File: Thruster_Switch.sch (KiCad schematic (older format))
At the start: 11 parts, among them P1 XT60, P2 XT60, P3 XT60, P4 XT60, Q2 IPD90P03P4L

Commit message: Update Netlist
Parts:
- renumbered D2 to D1, D3 to D2, Q2 to Q1, R3 to R1, R4 to R2, R5 to R3
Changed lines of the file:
@@
 AR Path="/58E6D43E/58E019DD" Ref="P11"  Part="1"
 AR Path="/58E0048C/58E019DD" Ref="P15"  Part="1"
-F 0 "P11" H 6850 4450 50  0000 C CNN
+F 0 "P15" H 6850 4450 50  0000 C CNN
 F 1 "XT60" H 6850 4150 50  0000 C CNN
 F 2 "zeabus:XT60" H 6950 4050 60  0001 C CNN
@@
 $EndComp
 $Comp
-L R R5
+L R R3
 U 1 1 58E01A68
 P 6250 4150
-AR Path="/58E52973/58E01A68" Ref="R5"  Part="1"
-AR Path="/58E62AD5/58E01A68" Ref="R20"  Part="1"
-AR Path="/58E6D43E/58E01A68" Ref="R25"  Part="1"
-AR Path="/58E0048C/58E01A68" Ref="R30"  Part="1"
-F 0 "R25" V 6330 4150 50  0000 C CNN
+AR Path="/58E52973/58E01A68" Ref="R3"  Part="1"
+AR Path="/58E62AD5/58E01A68" Ref="R12"  Part="1"
+AR Path="/58E6D43E/58E01A68" Ref="R15"  Part="1"
+AR Path="/58E0048C/58E01A68" Ref="R18"  Part="1"
+F 0 "R18" V 6330 4150 50  0000 C CNN
 F 1 "10k" V 6250 4150 50  0000 C CNN
 F 2 "Resistors_SMD:R_0603" V 6180 4150 50  0001 C CNN
@@
 $EndComp
 $Comp
-L LED_Small D3
+L LED_Small D2
 U 1 1 58E01A8B
 P 6250 4550
-AR Path="/58E52973/58E01A8B" Ref="D3"  Part="1"
-AR Path="/58E62AD5/58E01A8B" Ref="D10"  Part="1"
-AR Path="/58E6D43E/58E01A8B" Ref="D13"  Part="1"
-AR Path="/58E0048C/58E01A8B" Ref="D16"  Part="1"
-F 0 "D13" H 6200 4675 50  0000 L CNN
+AR Path="/58E52973/58E01A8B" Ref="D2"  Part="1"
+AR Path="/58E62AD5/58E01A8B" Ref="D8"  Part="1"
+AR Path="/58E6D43E/58E01A8B" Ref="D10"  Part="1"
+AR Path="/58E0048C/58E01A8B" Ref="D12"  Part="1"
+F 0 "D12" H 6200 4675 50  0000 L CNN
 F 1 "LED_Small" H 6075 4450 50  0000 L CNN
 F 2 "LEDs:LED_0603" V 6250 4550 50  0001 C CNN
@@
 $EndComp
 $Comp
-L R R3
+L R R1
 U 1 1 58E01FA8
 P 5550 2500
-AR Path="/58E52973/58E01FA8" Ref="R3"  Part="1"
-AR Path="/58E62AD5/58E01FA8" Ref="R18"  Part="1"
-AR Path="/58E6D43E/58E01FA8" Ref="R23"  Part="1"
-AR Path="/58E0048C/58E01FA8" Ref="R28"  Part="1"
-F 0 "R23" V 5630 2500 50  0000 C CNN
+AR Path="/58E52973/58E01FA8" Ref="R1"  Part="1"
+AR Path="/58E62AD5/58E01FA8" Ref="R10"  Part="1"
+AR Path="/58E6D43E/58E01FA8" Ref="R13"  Part="1"
+AR Path="/58E0048C/58E01FA8" Ref="R16"  Part="1"
+F 0 "R16" V 5630 2500 50  0000 C CNN
 F 1 "10k" V 5550 2500 50  0000 C CNN
 F 2 "Resistors_SMD:R_0603" V 5480 2500 50  0001 C CNN
@@
 $EndComp
 $Comp
-L R R4
+L R R2
 U 1 1 58E01FFB
 P 5550 3050
-AR Path="/58E52973/58E01FFB" Ref="R4"  Part="1"
-AR Path="/58E62AD5/58E01FFB" Ref="R19"  Part="1"
-AR Path="/58E6D43E/58E01FFB" Ref="R24"  Part="1"
-AR Path="/58E0048C/58E01FFB" Ref="R29"  Part="1"
-F 0 "R24" V 5630 3050 50  0000 C CNN
+AR Path="/58E52973/58E01FFB" Ref="R2"  Part="1"
+AR Path="/58E62AD5/58E01FFB" Ref="R11"  Part="1"
+AR Path="/58E6D43E/58E01FFB" Ref="R14"  Part="1"
+AR Path="/58E0048C/58E01FFB" Ref="R17"  Part="1"
+F 0 "R17" V 5630 3050 50  0000 C CNN
 F 1 "1k" V 5550 3050 50  0000 C CNN
 F 2 "Resistors_SMD:R_0603" V 5480 3050 50  0001 C CNN
@@
 $EndComp
 $Comp
-L GND #PWR012
+L GND #PWR12
 U 1 1 58E0369B
 P 6250 4800
-AR Path="/58E52973/58E0369B" Ref="#PWR012"  Part="1"
-AR Path="/58E62AD5/58E0369B" Ref="#PWR015"  Part="1"
-AR Path="/58E6D43E/58E0369B" Ref="#PWR016"  Part="1"
-AR Path="/58E0048C/58E0369B" Ref="#PWR017"  Part="1"
-F 0 "#PWR017" H 6250 4550 50  0001 C CNN
+AR Path="/58E52973/58E0369B" Ref="#PWR12"  Part="1"
+AR Path="/58E62AD5/58E0369B" Ref="#PWR15"  Part="1"
+AR Path="/58E6D43E/58E0369B" Ref="#PWR16"  Part="1"
+AR Path="/58E0048C/58E0369B" Ref="#PWR17"  Part="1"
+F 0 "#PWR17" H 6250 4550 50  0001 C CNN
 F 1 "GND" H 6250 4650 50  0000 C CNN
 F 2 "" H 6250 4800 50  0001 C CNN
@@
 AR Path="/58E6D43E/58E0D2A0" Ref="P12"  Part="1"
 AR Path="/58E0048C/58E0D2A0" Ref="P16"  Part="1"
-F 0 "P12" H 7400 4450 50  0000 C CNN
+F 0 "P16" H 7400 4450 50  0000 C CNN
 F 1 "XT60" H 7400 4150 50  0000 C CNN
 F 2 "zeabus:XT60" H 7500 4050 60  0001 C CNN
@@
 AR Path="/58E6D43E/58E0D2E8" Ref="P13"  Part="1"
 AR Path="/58E0048C/58E0D2E8" Ref="P17"  Part="1"
-F 0 "P13" H 7950 4450 50  0000 C CNN
+F 0 "P17" H 7950 4450 50  0000 C CNN
 F 1 "XT60" H 7950 4150 50  0000 C CNN
 F 2 "zeabus:XT60" H 8050 4050 60  0001 C CNN
@@
 AR Path="/58E6D43E/58E0D33F" Ref="P14"  Part="1"
 AR Path="/58E0048C/58E0D33F" Ref="P18"  Part="1"
-F 0 "P14" H 8500 4450 50  0000 C CNN
+F 0 "P18" H 8500 4450 50  0000 C CNN
 F 1 "XT60" H 8500 4150 50  0000 C CNN
 F 2 "zeabus:XT60" H 8600 4050 60  0001 C CNN
@@
 AR Path="/58E6D43E/58E4FE30" Ref="F5"  Part="1"
 AR Path="/58E0048C/58E4FE30" Ref="F6"  Part="1"
-F 0 "F5" V 6330 3550 50  0000 C CNN
+F 0 "F6" V 6330 3550 50  0000 C CNN
 F 1 "Fuse" V 6175 3550 50  0000 C CNN
 F 2 "zeabus:FUSE_AUTO" V 6180 3550 50  0001 C CNN
@@
 	6250 3700 6250 4000
 $Comp
-L Q_PMOS_GDS Q2
+L Q_PMOS_GDS Q1
 U 1 1 58E51C6A
 P 6150 3050
-AR Path="/58E52973/58E51C6A" Ref="Q2"  Part="1"
-AR Path="/58E62AD5/58E51C6A" Ref="Q8"  Part="1"
-AR Path="/58E6D43E/58E51C6A" Ref="Q10"  Part="1"
-AR Path="/58E0048C/58E51C6A" Ref="Q12"  Part="1"
-F 0 "Q10" H 6350 3100 50  0000 L CNN
+AR Path="/58E52973/58E51C6A" Ref="Q1"  Part="1"
+AR Path="/58E62AD5/58E51C6A" Ref="Q4"  Part="1"
+AR Path="/58E6D43E/58E51C6A" Ref="Q5"  Part="1"
+AR Path="/58E0048C/58E51C6A" Ref="Q6"  Part="1"
+F 0 "Q6" H 6350 3100 50  0000 L CNN
 F 1 "IPD90P03P4L" H 6350 3000 50  0000 L CNN
 F 2 "TO_SOT_Packages_SMD:TO-252-2Lead" H 6350 3150 50  0001 C CNN
@@
 $EndComp
 $Comp
-L D_Zener D2
+L D_Zener D1
 U 1 1 58E6427A
 P 5850 2750
-AR Path="/58E52973/58E6427A" Ref="D2"  Part="1"
-AR Path="/58E62AD5/58E6427A" Ref="D9"  Part="1"
-AR Path="/58E6D43E/58E6427A" Ref="D12"  Part="1"
-AR Path="/58E0048C/58E6427A" Ref="D15"  Part="1"
-F 0 "D12" H 5850 2850 50  0000 C CNN
+AR Path="/58E52973/58E6427A" Ref="D1"  Part="1"
+AR Path="/58E62AD5/58E6427A" Ref="D7"  Part="1"
+AR Path="/58E6D43E/58E6427A" Ref="D9"  Part="1"
+AR Path="/58E0048C/58E6427A" Ref="D11"  Part="1"
+F 0 "D11" H 5850 2850 50  0000 C CNN
 F 1 "BZX585-C12" H 5850 2650 50  0000 C CNN
 F 2 "Diodes_SMD:D_SOD-523" H 5850 2750 50  0001 C CNN

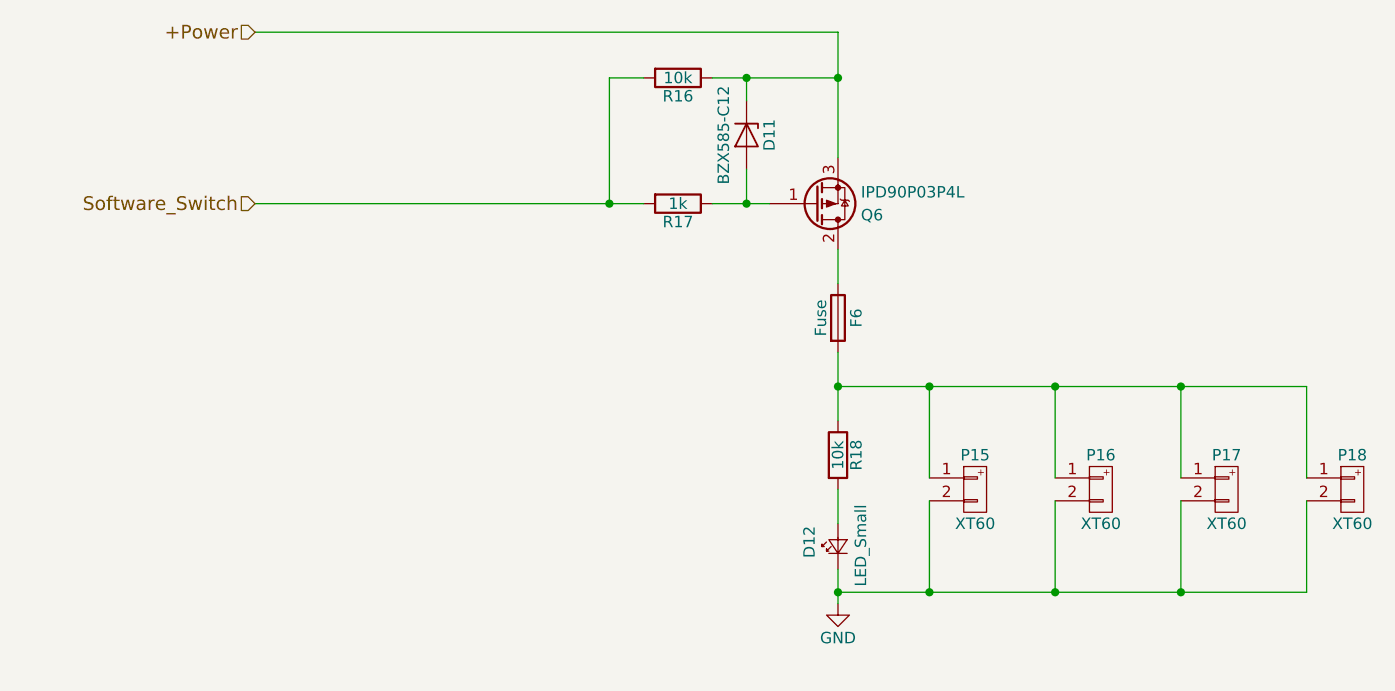
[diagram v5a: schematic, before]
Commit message: Ver1 Power_dist PCB
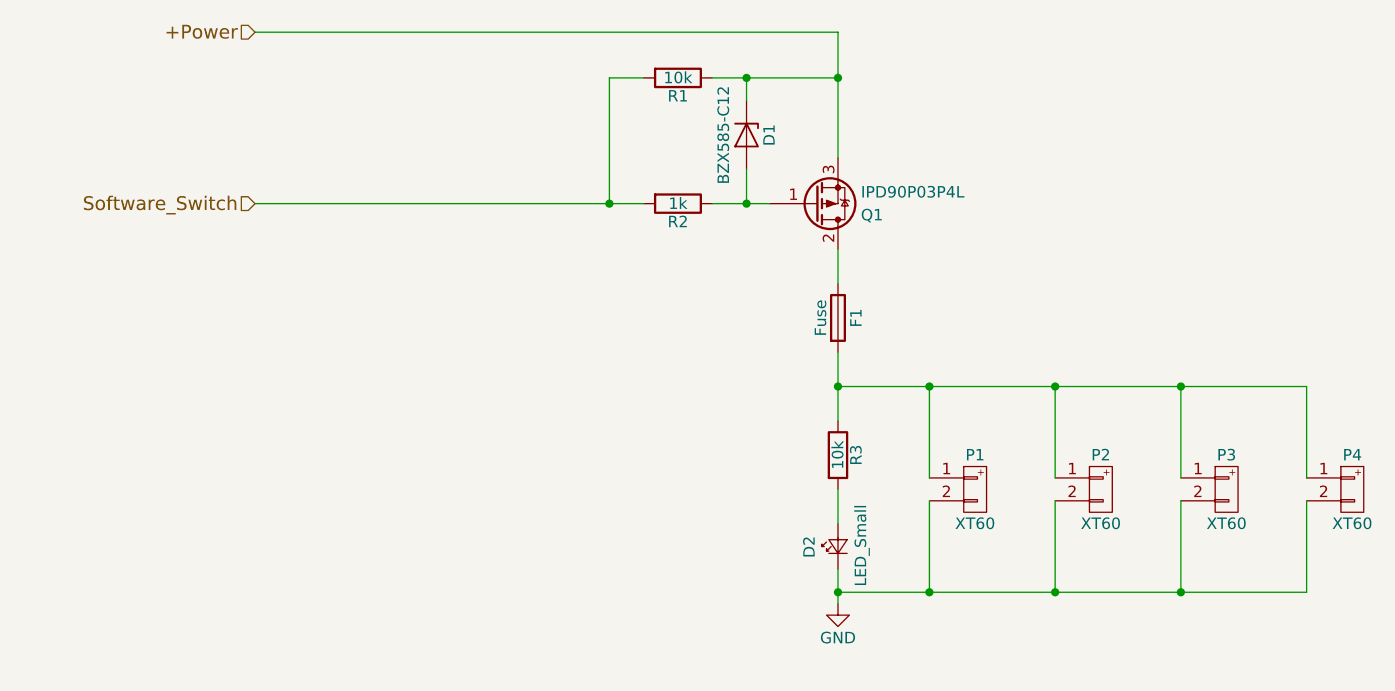
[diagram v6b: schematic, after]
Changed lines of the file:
@@
 $Descr A4 11693 8268
 encoding utf-8
-Sheet 6 10
+Sheet 2 9
 Title "Thruster Switch"
 Date "2017-04-06"
@@
 AR Path="/58E6D43E/58E019DD" Ref="P11"  Part="1"
 AR Path="/58E0048C/58E019DD" Ref="P15"  Part="1"
-F 0 "P15" H 6850 4450 50  0000 C CNN
+F 0 "P1" H 6850 4450 50  0000 C CNN
 F 1 "XT60" H 6850 4150 50  0000 C CNN
 F 2 "zeabus:XT60" H 6950 4050 60  0001 C CNN
@@
 AR Path="/58E6D43E/58E01A68" Ref="R15"  Part="1"
 AR Path="/58E0048C/58E01A68" Ref="R18"  Part="1"
-F 0 "R18" V 6330 4150 50  0000 C CNN
+F 0 "R3" V 6330 4150 50  0000 C CNN
 F 1 "10k" V 6250 4150 50  0000 C CNN
 F 2 "Resistors_SMD:R_0603" V 6180 4150 50  0001 C CNN
@@
 AR Path="/58E6D43E/58E01A8B" Ref="D10"  Part="1"
 AR Path="/58E0048C/58E01A8B" Ref="D12"  Part="1"
-F 0 "D12" H 6200 4675 50  0000 L CNN
+F 0 "D2" H 6200 4675 50  0000 L CNN
 F 1 "LED_Small" H 6075 4450 50  0000 L CNN
 F 2 "LEDs:LED_0603" V 6250 4550 50  0001 C CNN
@@
 AR Path="/58E6D43E/58E01FA8" Ref="R13"  Part="1"
 AR Path="/58E0048C/58E01FA8" Ref="R16"  Part="1"
-F 0 "R16" V 5630 2500 50  0000 C CNN
+F 0 "R1" V 5630 2500 50  0000 C CNN
 F 1 "10k" V 5550 2500 50  0000 C CNN
 F 2 "Resistors_SMD:R_0603" V 5480 2500 50  0001 C CNN
@@
 AR Path="/58E6D43E/58E01FFB" Ref="R14"  Part="1"
 AR Path="/58E0048C/58E01FFB" Ref="R17"  Part="1"
-F 0 "R17" V 5630 3050 50  0000 C CNN
+F 0 "R2" V 5630 3050 50  0000 C CNN
 F 1 "1k" V 5550 3050 50  0000 C CNN
 F 2 "Resistors_SMD:R_0603" V 5480 3050 50  0001 C CNN
@@
 AR Path="/58E6D43E/58E0369B" Ref="#PWR16"  Part="1"
 AR Path="/58E0048C/58E0369B" Ref="#PWR17"  Part="1"
-F 0 "#PWR17" H 6250 4550 50  0001 C CNN
+F 0 "#PWR12" H 6250 4550 50  0001 C CNN
 F 1 "GND" H 6250 4650 50  0000 C CNN
 F 2 "" H 6250 4800 50  0001 C CNN
@@
 AR Path="/58E6D43E/58E0D2A0" Ref="P12"  Part="1"
 AR Path="/58E0048C/58E0D2A0" Ref="P16"  Part="1"
-F 0 "P16" H 7400 4450 50  0000 C CNN
+F 0 "P2" H 7400 4450 50  0000 C CNN
 F 1 "XT60" H 7400 4150 50  0000 C CNN
 F 2 "zeabus:XT60" H 7500 4050 60  0001 C CNN
@@
 AR Path="/58E6D43E/58E0D2E8" Ref="P13"  Part="1"
 AR Path="/58E0048C/58E0D2E8" Ref="P17"  Part="1"
-F 0 "P17" H 7950 4450 50  0000 C CNN
+F 0 "P3" H 7950 4450 50  0000 C CNN
 F 1 "XT60" H 7950 4150 50  0000 C CNN
 F 2 "zeabus:XT60" H 8050 4050 60  0001 C CNN
@@
 AR Path="/58E6D43E/58E0D33F" Ref="P14"  Part="1"
 AR Path="/58E0048C/58E0D33F" Ref="P18"  Part="1"
-F 0 "P18" H 8500 4450 50  0000 C CNN
+F 0 "P4" H 8500 4450 50  0000 C CNN
 F 1 "XT60" H 8500 4150 50  0000 C CNN
 F 2 "zeabus:XT60" H 8600 4050 60  0001 C CNN
@@
 AR Path="/58E6D43E/58E4FE30" Ref="F5"  Part="1"
 AR Path="/58E0048C/58E4FE30" Ref="F6"  Part="1"
-F 0 "F6" V 6330 3550 50  0000 C CNN
+F 0 "F1" V 6330 3550 50  0000 C CNN
 F 1 "Fuse" V 6175 3550 50  0000 C CNN
 F 2 "zeabus:FUSE_AUTO" V 6180 3550 50  0001 C CNN
@@
 AR Path="/58E6D43E/58E51C6A" Ref="Q5"  Part="1"
 AR Path="/58E0048C/58E51C6A" Ref="Q6"  Part="1"
-F 0 "Q6" H 6350 3100 50  0000 L CNN
+F 0 "Q1" H 6350 3100 50  0000 L CNN
 F 1 "IPD90P03P4L" H 6350 3000 50  0000 L CNN
 F 2 "TO_SOT_Packages_SMD:TO-252-2Lead" H 6350 3150 50  0001 C CNN
@@
 AR Path="/58E6D43E/58E6427A" Ref="D9"  Part="1"
 AR Path="/58E0048C/58E6427A" Ref="D11"  Part="1"
-F 0 "D11" H 5850 2850 50  0000 C CNN
+F 0 "D1" H 5850 2850 50  0000 C CNN
 F 1 "BZX585-C12" H 5850 2650 50  0000 C CNN
 F 2 "Diodes_SMD:D_SOD-523" H 5850 2750 50  0001 C CNN
